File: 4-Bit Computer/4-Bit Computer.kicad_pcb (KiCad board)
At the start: 4 copper layers, 222.5 x 184.4 mm, 295 parts, among them J1 +12v, Q1 BC547, Q10 BC547, Q11 BC547, Q12 BC547, Q13 BC547, Q14 BC547, Q15 BC547, Q16 BC547, Q17 BC547, Q18 BC547, Q19 BC547, Q2 BC547, Q20 BC547, Q21 BC547, Q22 BC547, Q23 BC547, Q24 BC547, Q25 BC547, Q26 BC547, Q27 BC547, Q28 BC547, Q29 BC547, Q3 BC547, Q30 BC547, Q31 BC547, Q32 BC547, Q33 BC547, Q34 BC547, Q35 BC547, Q36 BC547, Q37 BC547, Q38 BC547, Q39 BC547, Q4 BC547, Q40 BC547, Q41 BC547, Q42 BC547, Q43 BC547, Q44 BC547, Q45 BC547, Q46 BC547, Q47 BC547, Q48 BC547, Q49 BC547, Q5 BC547, Q50 BC547, Q51 BC547, Q52 BC547, Q53 BC547, Q54 BC547, Q55 BC547, Q56 BC547, Q57 BC547, Q58 BC547, Q59 BC547, Q6 BC547, Q60 BC547, Q61 BC547, Q62 BC547, Q63 BC547, Q64 BC547, Q65 BC547, Q66 BC547, Q67 BC547, Q68 BC547, Q69 BC547, Q7 BC547, Q70 BC547, Q71 BC547, Q72 BC547, Q73 BC547, Q74 BC547, Q75 BC547, Q76 BC547, Q77 BC547, Q78 BC547, Q79 BC547, Q8 BC547, Q80 BC547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

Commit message: Cleanup...
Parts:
- DS1: value GREEN -> Adapter
- DS10, DS14, DS6: value BLUE -> 4
- DS11, DS15, DS7: value BLUE -> 8
- DS12, DS4, DS8: value BLUE -> 1
- DS13, DS5, DS9: value BLUE -> 2
- DS16: value BLUE -> 16
- DS2: value ORANGE -> Battery
- DS3: value RED -> Standby
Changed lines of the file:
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@@
       (effects (font (size 1 1) (thickness 0.15)))
     )
-    (fp_text value GREEN (at 0 -4.572) (layer F.SilkS)
+    (fp_text value Adapter (at 0 -4.572) (layer F.SilkS)
       (effects (font (size 1 1) (thickness 0.15)))
     )
@@
       (effects (font (size 1 1) (thickness 0.15)))
     )
-    (fp_text value ORANGE (at 0 -4.572) (layer F.SilkS)
+    (fp_text value Battery (at 0 -4.572) (layer F.SilkS)
       (effects (font (size 1 1) (thickness 0.15)))
     )
@@
       (effects (font (size 1 1) (thickness 0.15)))
     )
-    (fp_text value RED (at 0 -4.572) (layer F.SilkS)
+    (fp_text value Standby (at 0 -4.572) (layer F.SilkS)
       (effects (font (size 1 1) (thickness 0.15)))
     )
@@
       (effects (font (size 1 1) (thickness 0.15)))
     )
-    (fp_text value BLUE (at 0 -4.572) (layer F.SilkS)
+    (fp_text value 1 (at 0 -4.572) (layer F.SilkS)
       (effects (font (size 1 1) (thickness 0.15)))
     )
@@
       (effects (font (size 1 1) (thickness 0.15)))
     )
-    (fp_text value BLUE (at 0 -4.572) (layer F.SilkS)
+    (fp_text value 2 (at 0 -4.572) (layer F.SilkS)
       (effects (font (size 1 1) (thickness 0.15)))
     )
@@
       (effects (font (size 1 1) (thickness 0.15)))
     )
-    (fp_text value BLUE (at 0 -4.572) (layer F.SilkS)
+    (fp_text value 4 (at 0 -4.572) (layer F.SilkS)
       (effects (font (size 1 1) (thickness 0.15)))
     )
@@
       (effects (font (size 1 1) (thickness 0.15)))
     )
-    (fp_text value BLUE (at 0 -4.572) (layer F.SilkS)
+    (fp_text value 8 (at 0 -4.572) (layer F.SilkS)
       (effects (font (size 1 1) (thickness 0.15)))
     )
@@
       (effects (font (size 1 1) (thickness 0.15)))
     )
-    (fp_text value BLUE (at 0 -4.572) (layer F.SilkS)
+    (fp_text value 1 (at 0 -4.572) (layer F.SilkS)
       (effects (font (size 1 1) (thickness 0.15)))
     )
@@
       (effects (font (size 1 1) (thickness 0.15)))
     )
-    (fp_text value BLUE (at 0 -4.572) (layer F.SilkS)
+    (fp_text value 2 (at 0 -4.572) (layer F.SilkS)
       (effects (font (size 1 1) (thickness 0.15)))
     )
@@
       (effects (font (size 1 1) (thickness 0.15)))
     )
-    (fp_text value BLUE (at 0 -4.572) (layer F.SilkS)
+    (fp_text value 4 (at 0 -4.572) (layer F.SilkS)
       (effects (font (size 1 1) (thickness 0.15)))
     )
@@
       (effects (font (size 1 1) (thickness 0.15)))
     )
-    (fp_text value BLUE (at 0 -4.572) (layer F.SilkS)
+    (fp_text value 8 (at 0 -4.572) (layer F.SilkS)
       (effects (font (size 1 1) (thickness 0.15)))
     )
@@
       (effects (font (size 1 1) (thickness 0.15)))
     )
-    (fp_text value BLUE (at 0 -4.572) (layer F.SilkS)
+    (fp_text value 1 (at 0 -4.572) (layer F.SilkS)
       (effects (font (size 1 1) (thickness 0.15)))
     )
@@
       (effects (font (size 1 1) (thickness 0.15)))
     )
-    (fp_text value BLUE (at 0 -4.572) (layer F.SilkS)
+    (fp_text value 2 (at 0 -4.572) (layer F.SilkS)
       (effects (font (size 1 1) (thickness 0.15)))
     )
@@
       (effects (font (size 1 1) (thickness 0.15)))
     )
-    (fp_text value BLUE (at 0 -4.572) (layer F.SilkS)
+    (fp_text value 4 (at 0 -4.572) (layer F.SilkS)
       (effects (font (size 1 1) (thickness 0.15)))
     )
@@
       (effects (font (size 1 1) (thickness 0.15)))
     )
-    (fp_text value BLUE (at 0 -4.572) (layer F.SilkS)
+    (fp_text value 8 (at 0 -4.572) (layer F.SilkS)
       (effects (font (size 1 1) (thickness 0.15)))
     )
@@
       (effects (font (size 1 1) (thickness 0.15)))
     )
-    (fp_text value BLUE (at 0 -4.572) (layer F.SilkS)
-      (effects (font (size 1 1) (thickness 0.15)))
-    )
+    (fp_text value 16 (at 0 -4.572) (layer F.SilkS)
+      (effects (font (size 1 1) (thickness 0.15)))
+    )

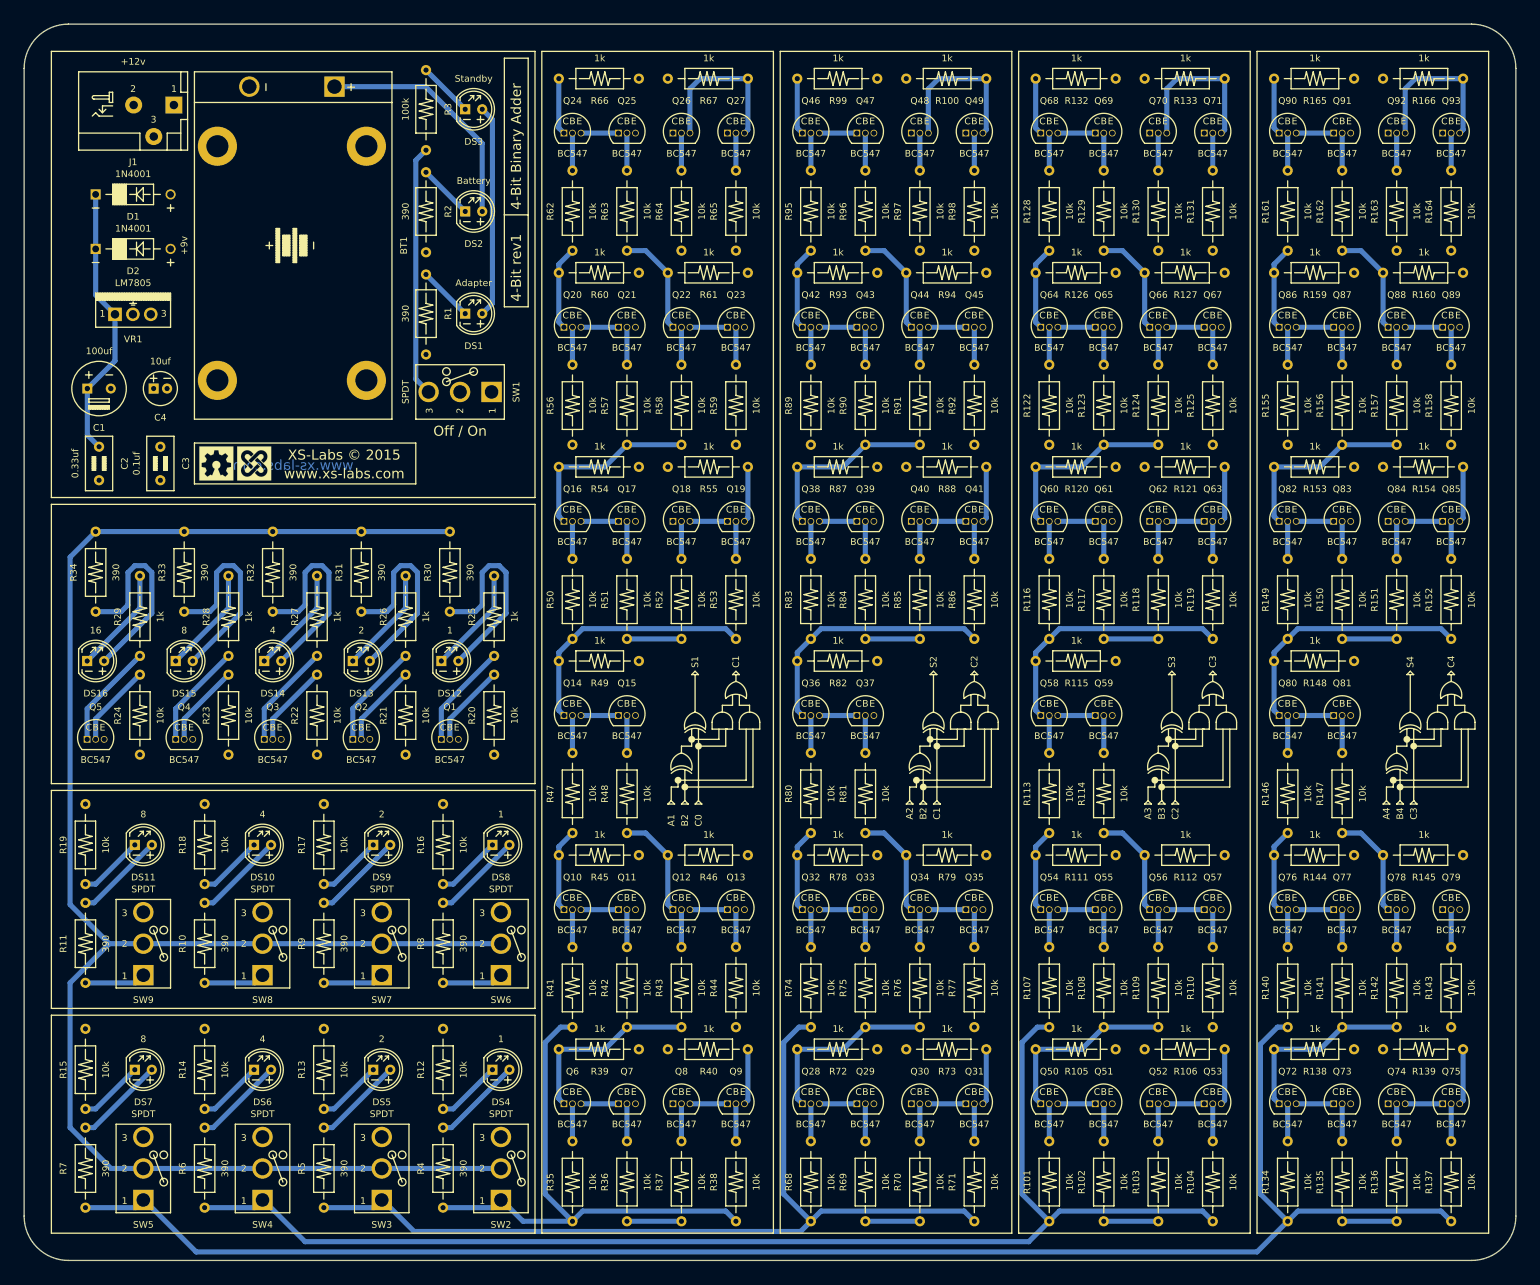
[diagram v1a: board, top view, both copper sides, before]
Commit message: Now using wide transistors - easier to solder.
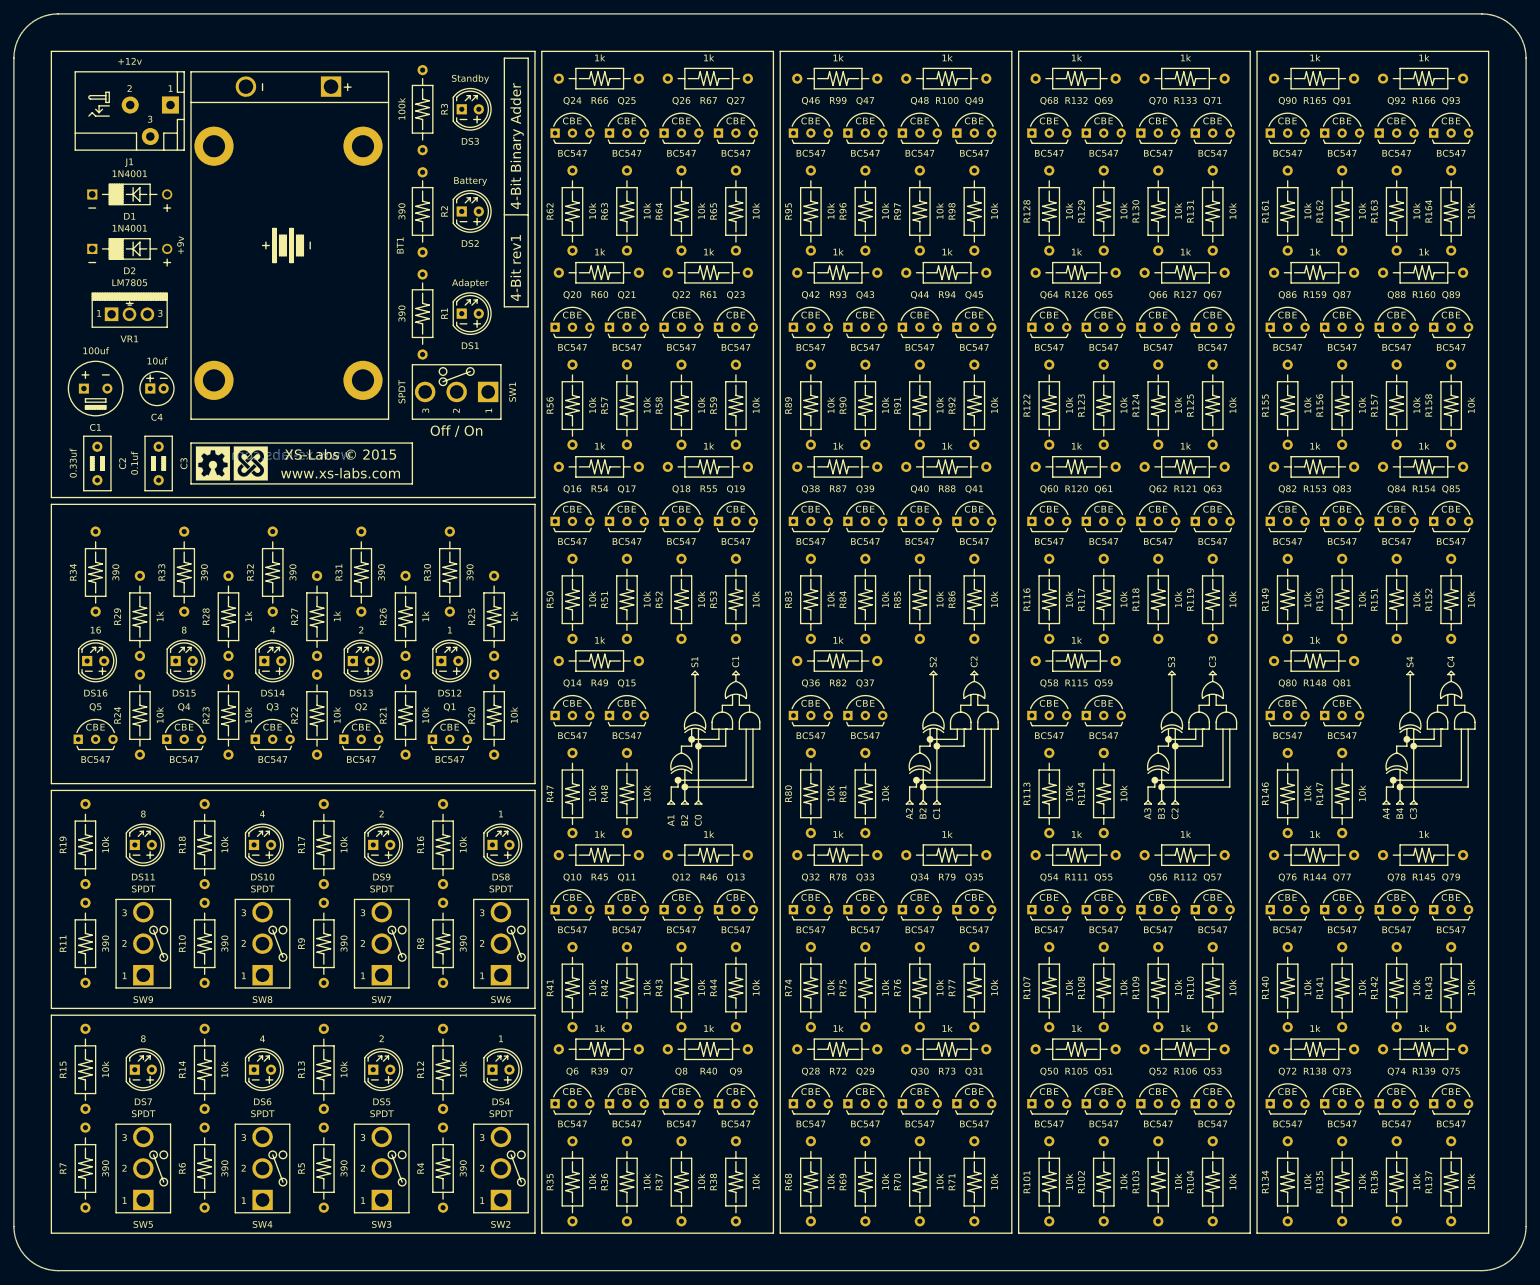
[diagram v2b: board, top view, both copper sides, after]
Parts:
- moved R1 0.51 mm to (98.0, 144.8)
- moved R2 0.51 mm to (98.0, 129.5)
- moved R3 0.51 mm to (98.0, 114.3)
- moved SW1 0.51 mm to (103.1, 156.5)
- moved BT1 0.51 mm to (78.2, 134.6)
- moved C1 0.51 mm to (49.3, 156.0)
- moved C4 0.51 mm to (58.4, 156.0)
- moved D1 0.51 mm to (54.4, 127.0)
- moved D2 0.51 mm to (54.4, 135.1)
- moved DS1 0.51 mm to (105.2, 144.8)
- moved DS2 0.51 mm to (105.2, 129.5)
- moved DS3 0.51 mm to (105.2, 114.3)
- moved G*** 0.51 mm to (78.2, 137.2)
- moved G*** 0.51 mm to (69.6, 167.1)
- moved J1 0.51 mm to (54.4, 113.8)
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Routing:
- net Net-(R30-Pad1): track 273.4 -> 0.00 mm
- net A4: track 243.8 -> 0.00 mm
- net A3: track 189.3 -> 0.00 mm
- net A2: track 134.7 -> 0.00 mm
- net A1: track 80.1 -> 0.00 mm
- net Net-(C1-Pad1): track 41.3 -> 0.00 mm
- net Net-(Q80-Pad1): track 38.2 -> 0.00 mm
- net Net-(Q58-Pad1): track 38.2 -> 0.00 mm
- net Net-(Q36-Pad1): track 38.2 -> 0.00 mm
- net Net-(Q14-Pad1): track 38.2 -> 0.00 mm
- net Net-(R3-Pad1): track 37.5 -> 0.00 mm
- net Net-(BT1-Pad1): track 35.7 -> 0.00 mm
- net Net-(D1-Pad2): track 32.4 -> 0.00 mm
- net /Adder 3/C3: track 32.3 -> 0.00 mm
- net /Adder 2/C2: track 32.3 -> 0.00 mm
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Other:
- board size 222.5 x 184.4 mm -> 225.6 x 187.5 mm
